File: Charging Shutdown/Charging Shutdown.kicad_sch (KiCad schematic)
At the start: 21 parts, among them J2 776280-1, K1 V23047A1012A511, K2 V23047A1012A511, K3 V23047A1012A511, Q1 2N2222, Q2 2N2222, Q3 2N2222

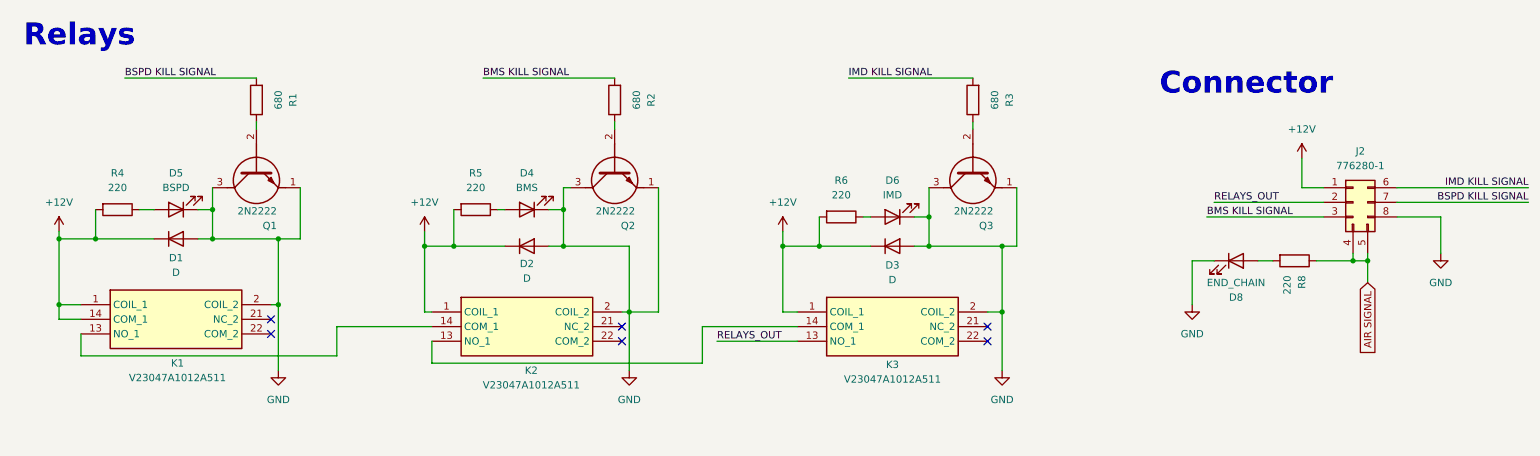
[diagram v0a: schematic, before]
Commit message: BSPD V1.2, Shutdown Circuit, Charging Shutdown Circuit, Voltage Indicator
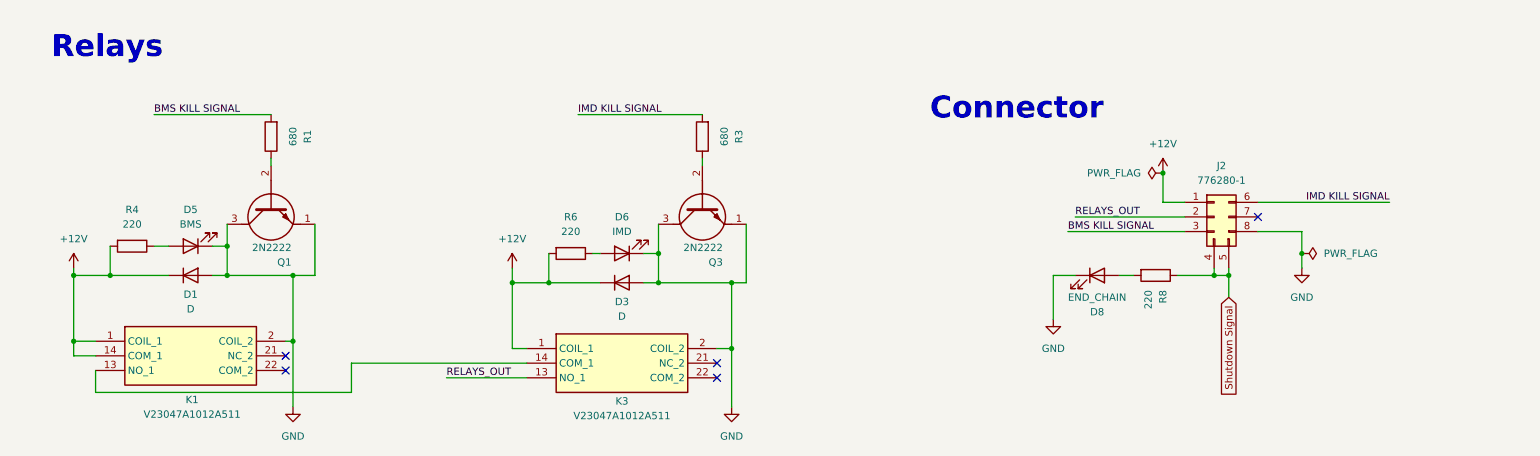
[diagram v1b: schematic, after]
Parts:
- removed D2: D, Diode_SMD:SODFL1608X70N, symbol Device:D
- removed D4: BMS, LED_SMD:LED_0603_1608Metric, symbol Device:LED
- removed K2: V23047A1012A511, Misc_footprints:V23047A1012A511, symbol V23047A1012A511:V23047A1012A511
- removed Q2: 2N2222, Package_TO_SOT_THT:2N2222, symbol Transistor_BJT:2N2222
- removed R2: 680, Resistor_SMD:R_0603_1608Metric, symbol Device:R
- removed R5: 220, Resistor_SMD:R_0603_1608Metric, symbol Device:R
- D5: value BSPD -> BMS; footprint LED_SMD:LED_0603_1608Metric -> LED_SMD:LED_0201_0603Metric
- D6, D8: footprint LED_SMD:LED_0603_1608Metric -> LED_SMD:LED_0201_0603Metric
- K1, K3: footprint Misc_footprints:V23047A1012A511 -> SDM_MiscFootprint:V23047A1012A511; symbol V23047A1012A511:V23047A1012A511 -> SDM_RELAY:V23047A1012A511
- Q1, Q3: footprint Package_TO_SOT_THT:2N2222 -> Shutdown_Footprint:2N2222; symbol Transistor_BJT:2N2222 -> SDM_Transistor:2N2222
- R1, R3, R4, R6, R8: footprint Resistor_SMD:R_0603_1608Metric -> Resistor_SMD:R_0201_0603Metric
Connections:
- net BMS KILL SIGNAL: now also R1.2
- net at K1.13 (NO_1): now also K3.14 (COM_1)
- net AIR SIGNAL renamed Shutdown Signal
- net BSPD KILL SIGNAL: no longer names the net of J2.7 (Pin_7)
- net BSPD KILL SIGNAL: no longer R1.2
- no-connect marks 6 -> 5
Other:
- moved on the sheet: D1, D3, D5, D6, D8, J2, K1, K3, Q1, Q3, R1, R3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

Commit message: BSPD, Shutdown/Charging Shutdown, & Voltage Indicator final changes
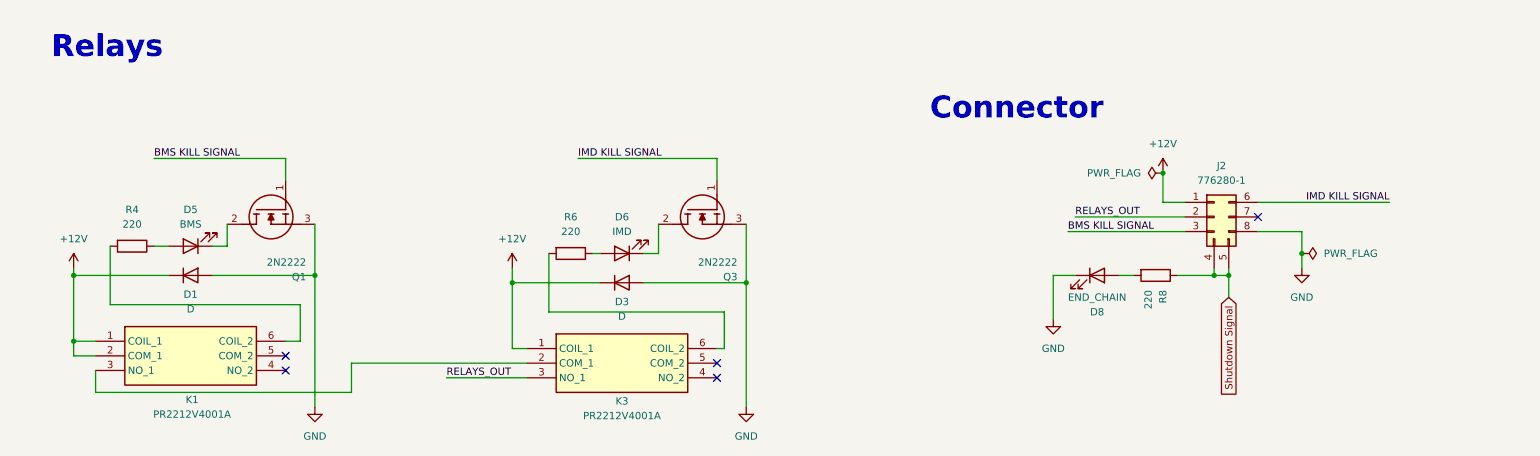
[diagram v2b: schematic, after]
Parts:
- removed R1, R3: 680, Resistor_SMD:R_0201_0603Metric, symbol Device:R
- K1, K3: value V23047A1012A511 -> PR2212V4001A; footprint SDM_MiscFootprint:V23047A1012A511 -> Shutdown_Footprint:PR2212V4001A; symbol SDM_RELAY:V23047A1012A511 -> Misc:PR22-12V-400-1A; Height 25.5 -> 16.1; Manufacturer_Name TE Connectivity -> Same Sky; Manufacturer_Part_Number V23047A1012A511 -> PR22-12V-400-1A
- Q1, Q3: footprint Shutdown_Footprint:2N2222 -> Shutdown_Footprint:ZXM61N02FTC; symbol SDM_Transistor:2N2222 -> Misc:ZXM61N02FTC; Arrow Part Number (none) -> ZXM61N02FTC; Arrow Price/Stock (none) -> https://www.arrow.com/en/products/zxm61n02ftc/diodes-incorp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; Height 5.31 -> 1.1; Manufacturer_Name NXP -> Diodes Incorporated; Manufacturer_Part_Number 2N2222 -> ZXM61N02FTC; Mouser Part Number (none) -> 522-ZXM61N02FTC; Mouser Price/Stock (none) -> https://www.mouser.co.uk/ProductDetail/Diodes-Incorporated/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
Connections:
- net +12V: now also K1.2 (COM_1); no longer K1.14 (COM_1), R4.2, R6.2
- net BMS KILL SIGNAL: now also Q1.1 (G)
- net GND: no longer D5.1 (K), D6.1 (K), K1.2 (COIL_2), K3.2 (COIL_2), Q1.1 (E), Q3.1 (E)
- net IMD KILL SIGNAL: now also Q3.1 (G)
- net RELAYS_OUT: now also K3.3 (NO_1); no longer K3.13 (NO_1)
- net at Q3.2 (D): now also D6.1 (K)
- net at Q1.2 (D): now also D5.1 (K)
- new net: K1.6 (COIL_2), R4.2
- new net: K1.3 (NO_1), K3.2 (COM_1)
- new net: K3.6 (COIL_2), R6.2
